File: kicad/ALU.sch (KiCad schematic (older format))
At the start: 7 parts, among them U1 74LS86, U2 74LS86, U3 74LS283, U4 74LS283, U5 7402, U6 74LS245, U7 74LS08

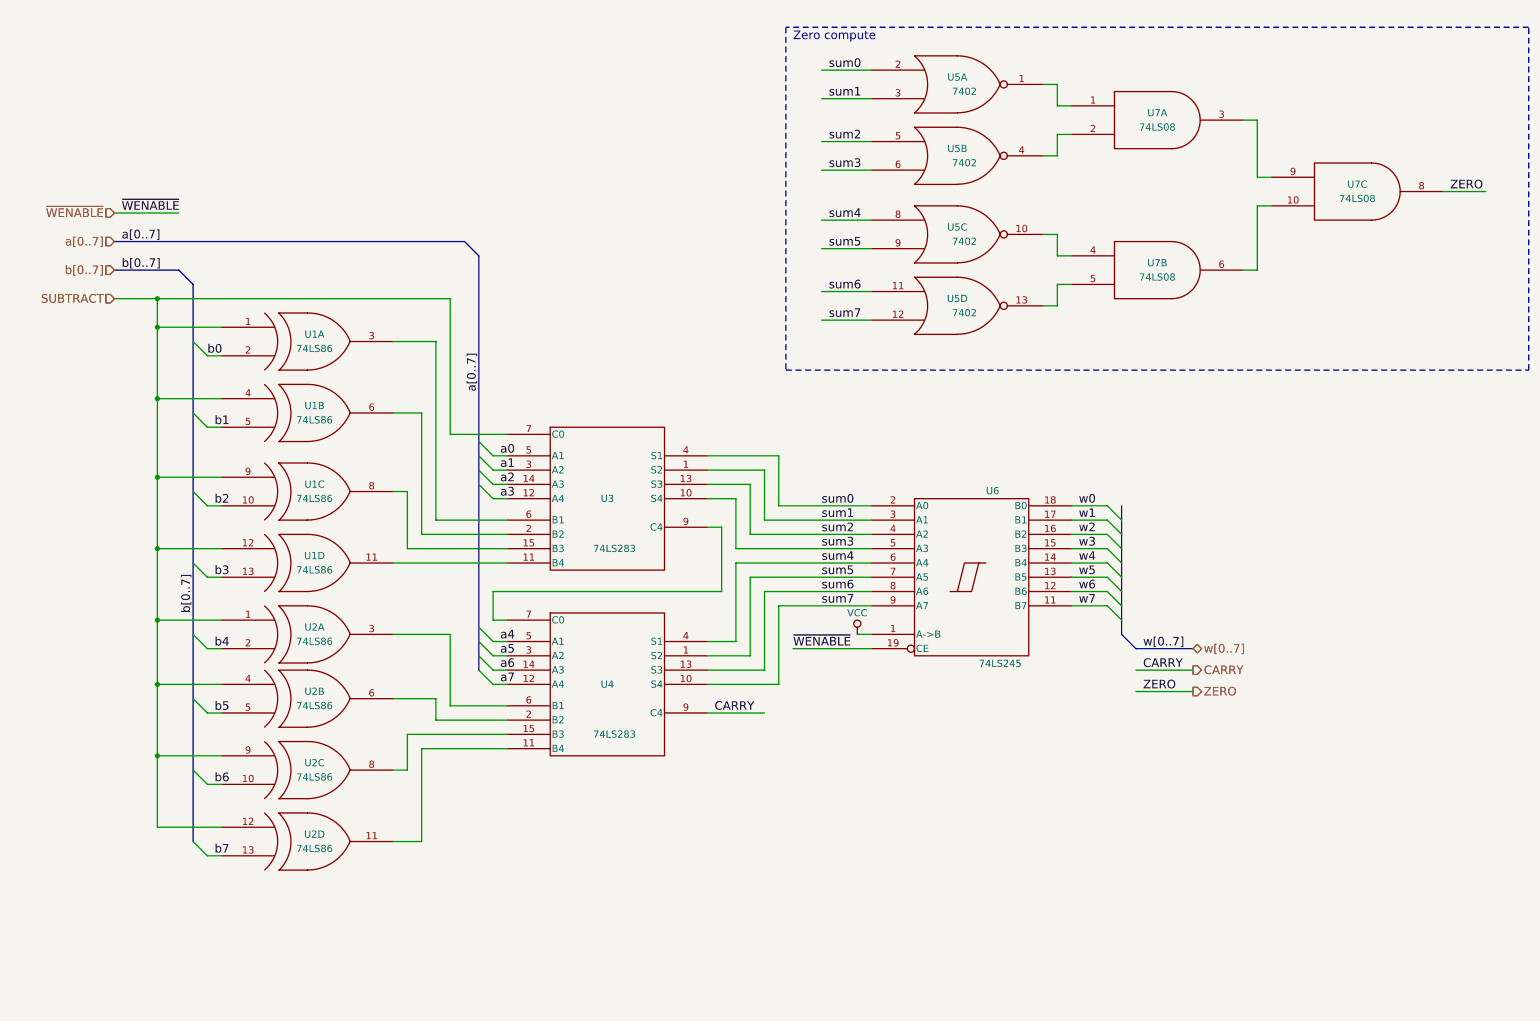
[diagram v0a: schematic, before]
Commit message: Update bugfix version to use updated kicad libraries
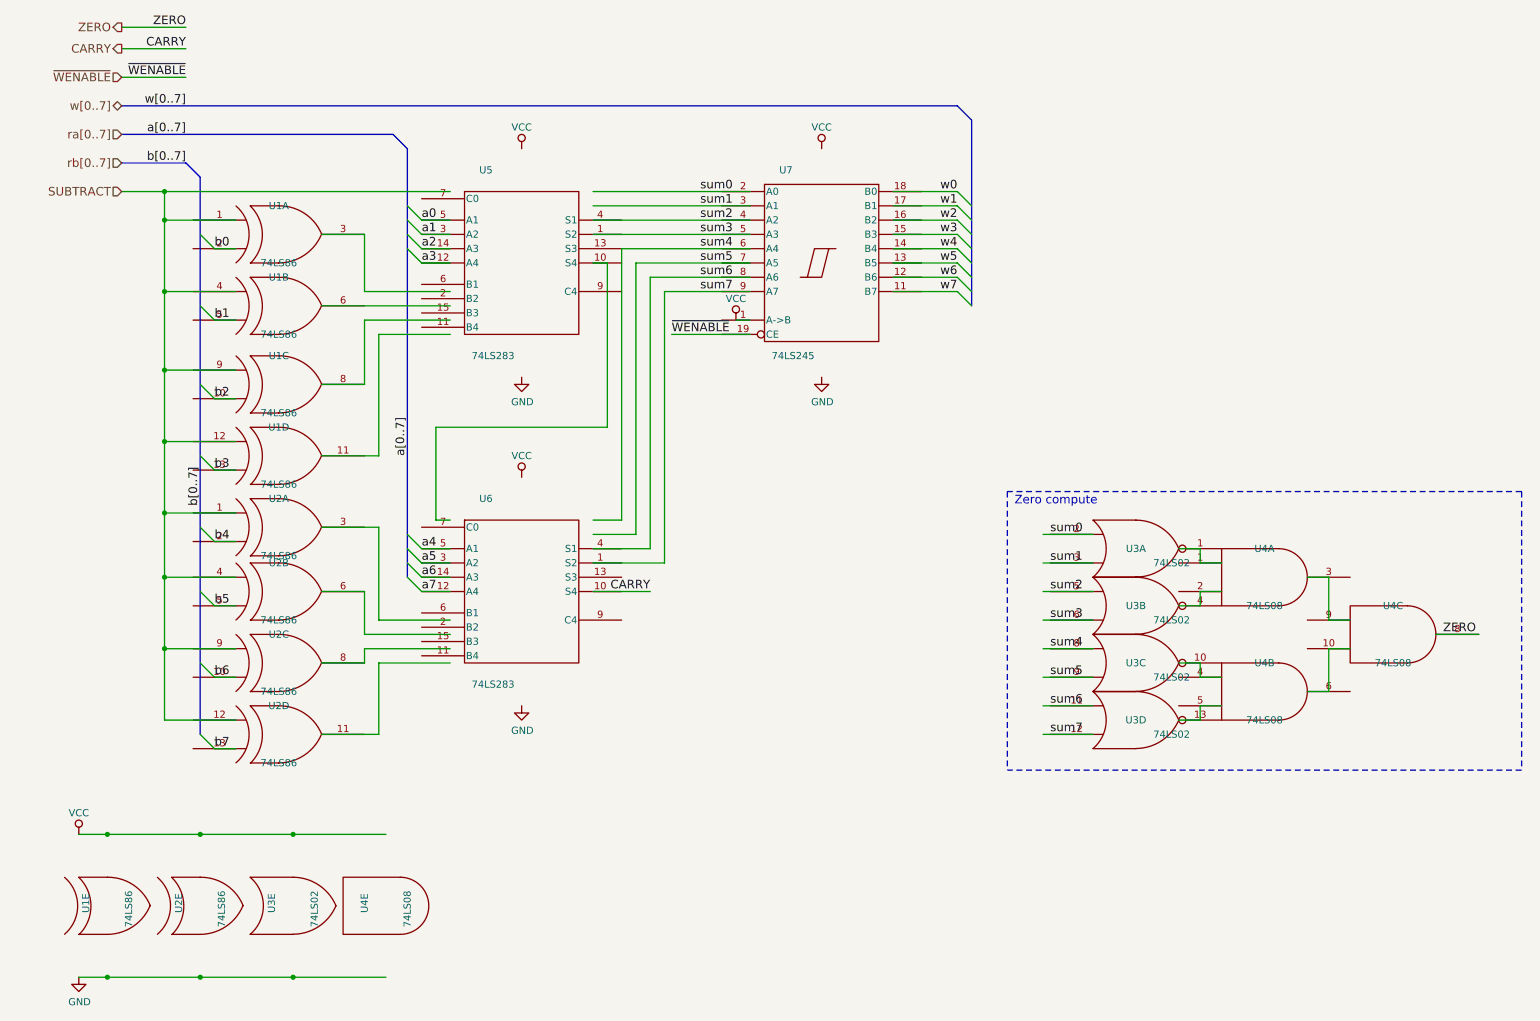
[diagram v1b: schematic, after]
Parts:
- removed U1, U2: 74LS86, Housings_DIP:DIP-14_W7.62mm_LongPads, symbol 74LS86
- removed U3, U4: 74LS283, Housings_DIP:DIP-16_W7.62mm_LongPads, symbol 74LS283
- removed U5: 7402, symbol 7402
- removed U6: 74LS245, Housings_DIP:DIP-20_W7.62mm_LongPads, symbol 74LS245
- removed U7: 74LS08, symbol 74LS08
- added U1, U2: 74LS86, symbol 74xx:74LS86
- added U3: 74LS02, symbol 74xx:74LS02
- added U4: 74LS08, symbol 74xx:74LS08
- added U5, U6: 74LS283, symbol 74xx:74LS283
- added U7: 74LS245, symbol 74xx:74LS245
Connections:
- net labels added: GND, ra[0..7], rb[0..7]
- wire segments 120 -> 126
